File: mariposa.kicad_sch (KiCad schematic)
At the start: 31 parts, among them J1 Conn_01x28_MountingPin, J3 Conn_ARM_SWD_TagConnect_TC203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, J6 Conn_01x10_MountingPin, SW1 SW_Push, SW3 SW_Push, Y1 CFPX-217 32.768KHz

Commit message: minor tweaks
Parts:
- Y1: value CFPX-217 32.768KHz -> CFPX-217 32.768KHz 9pF
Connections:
- net at Y1.1: now also MDBT1.34 (P0.00/XL1); no longer MDBT1.36 (P0.01/XL2)
- net at Y1.2: now also MDBT1.36 (P0.01/XL2); no longer MDBT1.34 (P0.00/XL1)
- no-connect marks 4 -> 7
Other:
- moved on the sheet: C19, J3, L2, L3, TP5, Y1

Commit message: fixes
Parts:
- D1: footprint PCM_LED_SMD_AKL:LED_0603_1608Metric -> PCM_LED_SMD_AKL:LED_0805_2012Metric
- R8: footprint Resistor_SMD:R_0603_1608Metric -> Resistor_SMD:R_0805_2012Metric
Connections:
- net VBUS: no longer C48.2
- net at Y1.1: now also MDBT1.36 (P0.01/XL2); no longer MDBT1.34 (P0.00/XL1)
- net at Y1.2: now also MDBT1.34 (P0.00/XL1); no longer MDBT1.36 (P0.01/XL2)
- net nrf_vbus: now reaches MDBT1.44 (VBUS), R21.1
- net nrf_vbus: now also C48.2
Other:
- moved on the sheet: C48, R21, Y1
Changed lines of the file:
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@@
 	)
 	(junction
-		(at 149.86 104.14)
+		(at 139.7 96.52)
 		(diameter 0)
 		(color 0 0 0 0)
@@
 	(wire
 		(pts
-			(xy 146.05 104.14) (xy 149.86 104.14)
+			(xy 139.7 96.52) (xy 147.32 96.52)
 		)
 		(stroke
@@
 	(wire
 		(pts
-			(xy 120.65 96.52) (xy 149.86 96.52)
+			(xy 120.65 96.52) (xy 139.7 96.52)
+		)
+		(stroke
+			(width 0)
+			(type default)
+		)
+	)
+	(wire
+		(pts
+			(xy 147.32 104.14) (xy 152.4 104.14)
 		)
 		(stroke
@@
 		)
 	)
+	(label "nrf_vbus"
+		(at 130.81 96.52 270)
+		(effects
+			(font
+				(size 1.27 1.27)
+			)
+			(justify right bottom)
+		)
+	)
 	(global_label "ch16"
 		(shape input)
@@
 		(length 2.54)
 		(shape diamond)
-		(at 149.86 104.14 270)
+		(at 147.32 104.14 180)
 		(fields_autoplaced yes)
 		(effects
@@
 		)
 		(property "Netclass" "power"
-			(at 152.4 102.9335 90)
+			(at 148.5265 106.68 0)
 			(effects
 				(font
@@
 			)
 		)
-		(property "Footprint" "PCM_LED_SMD_AKL:LED_0603_1608Metric"
+		(property "Footprint" "PCM_LED_SMD_AKL:LED_0805_2012Metric"
 			(at 81.28 173.99 0)
 			(effects
@@
 	(symbol
 		(lib_id "Device:Crystal")
-		(at 86.36 137.16 0)
+		(at 86.36 137.16 180)
 		(unit 1)
 		(exclude_from_sim no)
@@
 		(dnp no)
 		(property "Reference" "Y1"
-			(at 87.63 133.35 0)
+			(at 85.09 140.97 0)
 			(effects
 				(font
@@
 		)
 		(property "Value" "CFPX-217 32.768KHz 9pF"
-			(at 101.346 141.732 0)
+			(at 71.374 132.588 0)
 			(effects
 				(font
@@
 	(symbol
 		(lib_id "power:Earth")
-		(at 146.05 111.76 0)
+		(at 139.7 104.14 0)
 		(unit 1)
 		(exclude_from_sim no)
@@
 		(fields_autoplaced yes)
 		(property "Reference" "#PWR0103"
-			(at 146.05 118.11 0)
+			(at 139.7 110.49 0)
 			(effects
 				(font
@@
 		)
 		(property "Value" "GND"
-			(at 146.05 116.84 0)
+			(at 139.7 109.22 0)
 			(effects
 				(font
@@
 		)
 		(property "Footprint" ""
-			(at 146.05 111.76 0)
+			(at 139.7 104.14 0)
 			(effects
 				(font
@@
 		)
 		(property "Datasheet" "~"
-			(at 146.05 111.76 0)
+			(at 139.7 104.14 0)
 			(effects
 				(font
@@
 		)
 		(property "Description" "Power symbol creates a global label with name \"Earth\""
-			(at 146.05 111.76 0)
+			(at 139.7 104.14 0)
 			(effects
 				(font
@@
 	(symbol
 		(lib_id "power:VBUS")
-		(at 149.86 104.14 180)
+		(at 152.4 104.14 0)
 		(unit 1)
 		(exclude_from_sim no)
@@
 		(dnp no)
 		(property "Reference" "#PWR063"
-			(at 149.86 100.33 0)
+			(at 152.4 107.95 0)
 			(effects
 				(font
@@
 		)
 		(property "Value" "VBUS"
-			(at 149.86 109.22 90)
+			(at 152.4 99.06 90)
 			(effects
 				(font
@@
 		)
 		(property "Footprint" ""
-			(at 149.86 104.14 0)
+			(at 152.4 104.14 0)
 			(effects
 				(font
@@
 		)
 		(property "Datasheet" ""
-			(at 149.86 104.14 0)
+			(at 152.4 104.14 0)
 			(effects
 				(font
@@
 		)
 		(property "Description" "Power symbol creates a global label with name \"VBUS\""
-			(at 149.86 104.14 0)
+			(at 152.4 104.14 0)
 			(effects
 				(font
@@
 	(symbol
 		(lib_id "Device:R_US")
-		(at 149.86 100.33 0)
+		(at 147.32 100.33 0)
 		(unit 1)
 		(exclude_from_sim no)
@@
 		(dnp no)
 		(property "Reference" "R21"
-			(at 145.542 100.33 90)
+			(at 143.002 100.33 90)
 			(effects
 				(font
@@
 		)
 		(property "Value" "R2.2"
-			(at 147.574 100.33 90)
+			(at 145.034 100.33 90)
 			(effects
 				(font
@@
 		)
 		(property "Footprint" "Resistor_SMD:R_0805_2012Metric"
-			(at 150.876 100.584 90)
+			(at 148.336 100.584 90)
 			(effects
 				(font
@@
 		)
 		(property "Datasheet" "~"
-			(at 149.86 100.33 0)
+			(at 147.32 100.33 0)
 			(effects
 				(font
@@
 		)
 		(property "Description" "Resistor, US symbol"
-			(at 149.86 100.33 0)
+			(at 147.32 100.33 0)
 			(effects
 				(font
@@
 	(symbol
 		(lib_id "Device:C")
-		(at 146.05 107.95 180)
+		(at 139.7 100.33 180)
 		(unit 1)
 		(exclude_from_sim no)
@@
 		(dnp no)
 		(property "Reference" "C48"
-			(at 138.938 107.188 0)
+			(at 132.588 99.568 0)
 			(effects
 				(font
@@
 		)
 		(property "Value" "4.7uF"
-			(at 138.176 109.22 0)
+			(at 131.826 101.6 0)
 			(effects
 				(font
@@
 		)
 		(property "Footprint" "Capacitor_SMD:C_1206_3216Metric"
-			(at 145.0848 104.14 0)
+			(at 138.7348 96.52 0)
 			(effects
 				(font
@@
 		)
 		(property "Datasheet" "~"
-			(at 146.05 107.95 0)
+			(at 139.7 100.33 0)
 			(effects
 				(font
@@
 		)
 		(property "Description" "Unpolarized capacitor"
-			(at 146.05 107.95 0)
+			(at 139.7 100.33 0)
 			(effects
 				(font
@@
 			)
 		)
-		(property "Footprint" "Resistor_SMD:R_0603_1608Metric"
+		(property "Footprint" "Resistor_SMD:R_0805_2012Metric"
 			(at 73.406 175.006 90)
 			(effects

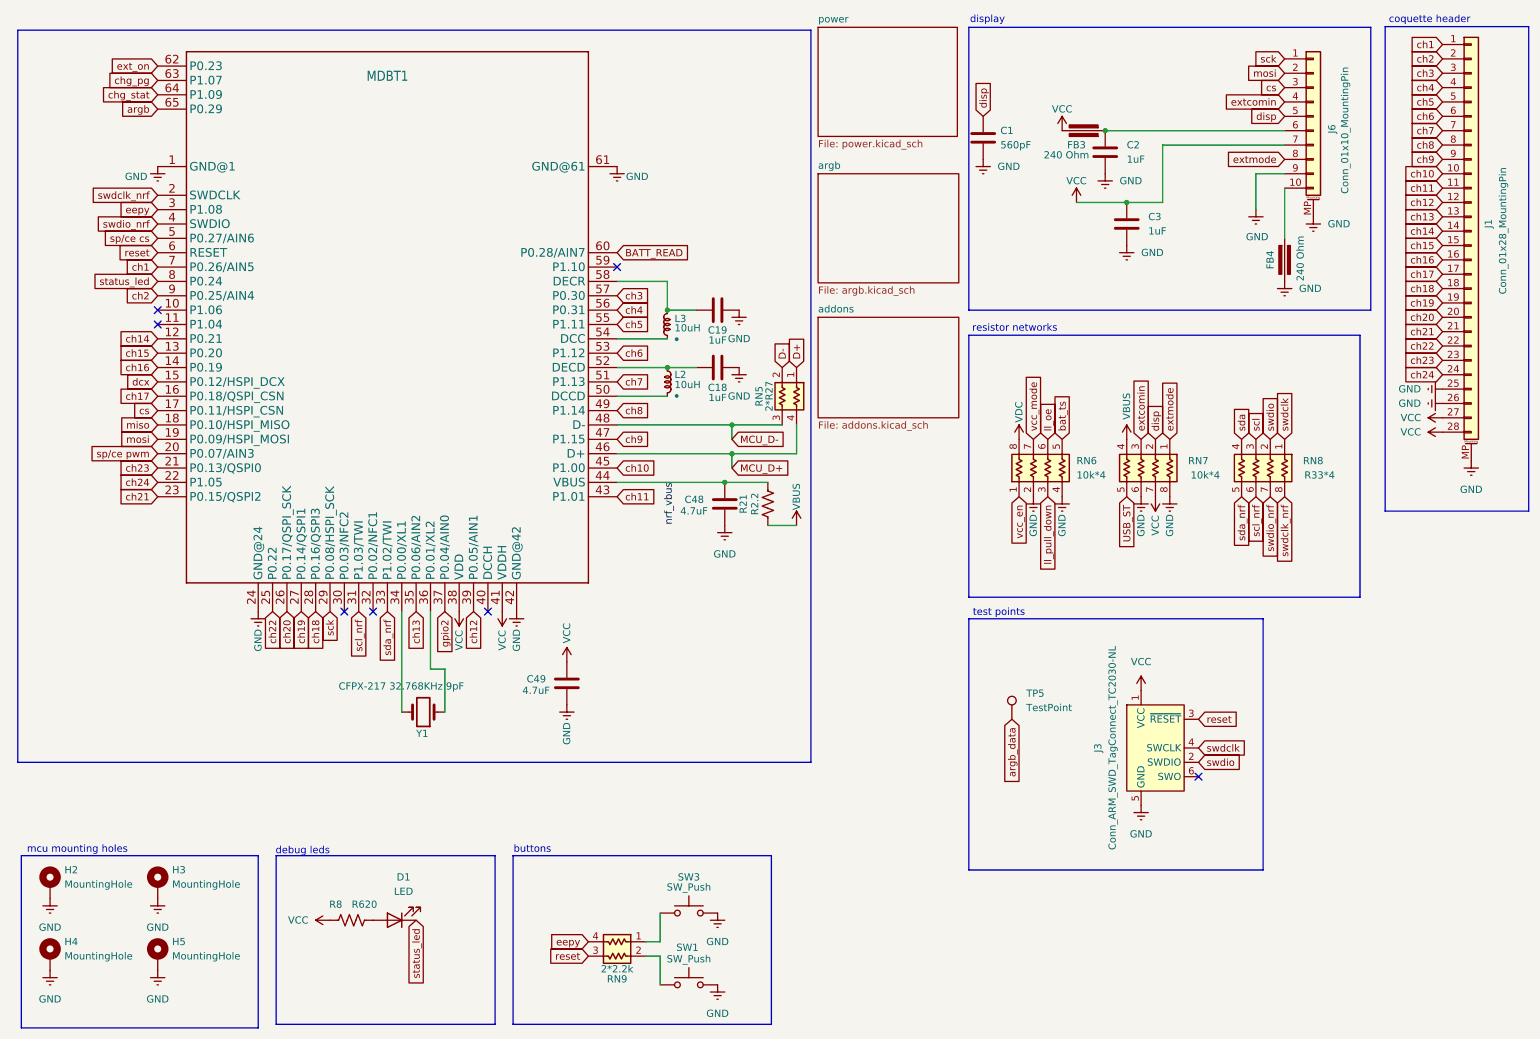
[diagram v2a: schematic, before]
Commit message: trying stm32 layout
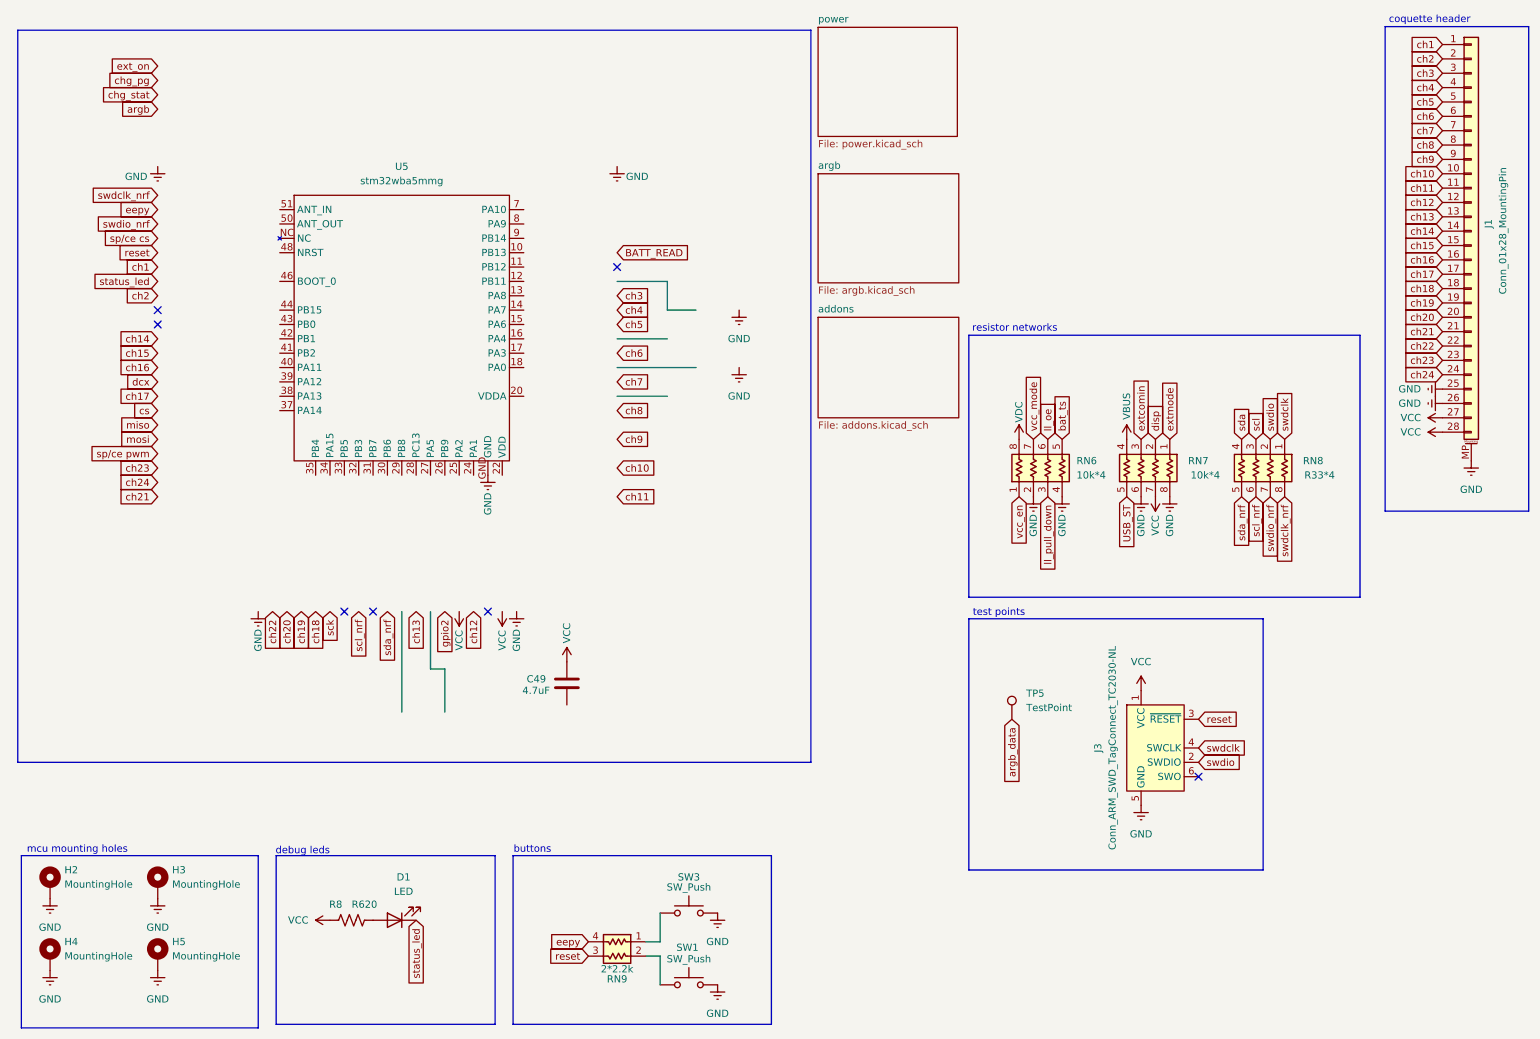
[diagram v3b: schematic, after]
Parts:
- removed C1: 560pF, Capacitor_SMD:C_0603_1608Metric, symbol Device:C
- removed C18, C19, C2, C3: 1uF, Capacitor_SMD:C_0603_1608Metric, symbol Device:C
- removed C48: 4.7uF, Capacitor_SMD:C_1206_3216Metric, symbol Device:C
- removed FB3, FB4: 240 Ohm, PCM_Ferrite_SMD_AKL:Ferrite_0805_2012Metric, symbol PCM_Device_AKL:Ferrite_Bead
- removed J6: Conn_01x10_MountingPin, Connector_FFC-FPC:Hirose_FH12-10S-0.5SH_1x10-1MP_P0.50mm_Horizontal, symbol Connector_Generic_MountingPin:Conn_01x10_MountingPin
- removed L2, L3: 10uH, Inductor_SMD:L_0603_1608Metric, symbol PCM_Generic-50:L,IEEE
- removed MDBT1: ~, coquette_footprints:MDBT53, symbol coquette_symbols:MDBT53
- removed R21: R2.2, Resistor_SMD:R_0805_2012Metric, symbol Device:R_US
- removed RN5: 2*R27, Resistor_SMD:R_Array_Convex_2x0603, symbol PCM_Resistor_US_AKL:R_2x0402_Convex
- removed Y1: CFPX-217 32.768KHz 9pF, Crystal:Crystal_SMD_3215-2Pin_3.2x1.5mm, symbol Device:Crystal
- added U5: stm32wba5mmg, coquette_footprints:stm32wba5mmg, symbol coquette_symbols:stm32wba5mmg
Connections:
- net GND: now also U5.GND; no longer C49.1
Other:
- note removed: "display"
